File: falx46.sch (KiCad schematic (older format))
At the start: 124 parts, among them J1 USB_C_Receptacle_USB2.0, J2 OLED_I2C, J3 AVR-ISP-6, J4 TRRS_I2C, SW1 SW_PUSH, SW10 SW_PUSH, SW11 SW_PUSH, SW12 SW_PUSH, SW13 SW_PUSH, SW14 SW_PUSH, SW15 SW_PUSH, SW16 SW_PUSH, SW17 SW_PUSH, SW18 SW_PUSH, SW19 Rotary_Encoder_Switch, SW2 SW_PUSH, SW20 SW_PUSH, SW21 SW_PUSH, SW22 SW_PUSH, SW23 SW_PUSH, SW24 SW_PUSH, SW25 SW_PUSH, SW26 SW_PUSH, SW27 SW_PUSH, SW28 SW_PUSH, SW29 SW_PUSH, SW3 SW_PUSH, SW30 SW_PUSH, SW31 SW_PUSH, SW32 SW_PUSH, SW33 SW_PUSH, SW34 SW_PUSH, SW35 SW_PUSH, SW36 Rotary_Encoder_Switch, SW37 SW_PUSH, SW38 SW_PUSH, SW39 SW_PUSH, SW4 SW_PUSH, SW40 SW_PUSH, SW41 SW_PUSH, SW42 SW_PUSH, SW43 SW_PUSH, SW44 SW_PUSH, SW45 SW_PUSH, SW46 SW_PUSH, SW47 SW_Push, SW5 SW_PUSH, SW6 SW_PUSH, SW7 SW_PUSH, SW8 SW_PUSH, SW9 SW_PUSH, U1 ATmega32U4-AU, Y1 16MHz

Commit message: ライブラリの参照を修正
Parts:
- J4: symbol falx46-rescue:MJ-4PP-9-kbd -> foostan_kbd:MJ-4PP-9
- SW1, SW10, SW11, SW12, SW13, SW14, SW15, SW16, SW17, SW18, SW2, SW20, SW21, SW22, SW23, SW24, SW25, SW26, SW27, SW28, SW29, SW3, SW30, SW31, SW32, SW33, SW34, SW35, SW37, SW38, SW39, SW4, SW40, SW41, SW42, SW43, SW44, SW45, SW46, SW5, SW6, SW7, SW8, SW9: symbol falx46-rescue:SW_PUSH-kbd -> foostan_kbd:SW_PUSH
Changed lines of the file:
@@
 COL0
 $Comp
-L falx46-rescue:SW_PUSH-kbd SW1
+L foostan_kbd:SW_PUSH SW1
 U 1 1 5F5B60E2
 P 7450 1400
@@
 $EndComp
 $Comp
-L falx46-rescue:SW_PUSH-kbd SW2
+L foostan_kbd:SW_PUSH SW2
 U 1 1 5F5B6E67
 P 8250 1400
@@
 $EndComp
 $Comp
-L falx46-rescue:SW_PUSH-kbd SW3
+L foostan_kbd:SW_PUSH SW3
 U 1 1 5F5B876D
 P 9050 1400
@@
 $EndComp
 $Comp
-L falx46-rescue:SW_PUSH-kbd SW4
+L foostan_kbd:SW_PUSH SW4
 U 1 1 5F5B8EE0
 P 9850 1400
@@
 $EndComp
 $Comp
-L falx46-rescue:SW_PUSH-kbd SW5
+L foostan_kbd:SW_PUSH SW5
 U 1 1 5F5D5213
 P 10650 1400
@@
 COL6
 $Comp
-L falx46-rescue:SW_PUSH-kbd SW6
+L foostan_kbd:SW_PUSH SW6
 U 1 1 5F5D7903
 P 6600 2100
@@
 $EndComp
 $Comp
-L falx46-rescue:SW_PUSH-kbd SW7
+L foostan_kbd:SW_PUSH SW7
 U 1 1 5F5D856F
 P 7450 2100
@@
 $EndComp
 $Comp
-L falx46-rescue:SW_PUSH-kbd SW8
+L foostan_kbd:SW_PUSH SW8
 U 1 1 5F5D8D10
 P 8250 2100
@@
 $EndComp
 $Comp
-L falx46-rescue:SW_PUSH-kbd SW9
+L foostan_kbd:SW_PUSH SW9
 U 1 1 5F5D95B6
 P 9050 2100
@@
 $EndComp
 $Comp
-L falx46-rescue:SW_PUSH-kbd SW10
+L foostan_kbd:SW_PUSH SW10
 U 1 1 5F5D9E13
 P 9850 2100
@@
 $EndComp
 $Comp
-L falx46-rescue:SW_PUSH-kbd SW11
+L foostan_kbd:SW_PUSH SW11
 U 1 1 5F5DB97E
 P 10650 2100
@@
 $EndComp
 $Comp
-L falx46-rescue:SW_PUSH-kbd SW12
+L foostan_kbd:SW_PUSH SW12
 U 1 1 5F5DC0BA
 P 11450 2100
@@
 	6300 1100 6300 2100
 $Comp
-L falx46-rescue:SW_PUSH-kbd SW13
+L foostan_kbd:SW_PUSH SW13
 U 1 1 5F5F3D5F
 P 6600 2750
@@
 $EndComp
 $Comp
-L falx46-rescue:SW_PUSH-kbd SW14
+L foostan_kbd:SW_PUSH SW14
 U 1 1 5F5F4155
 P 7450 2750
@@
 $EndComp
 $Comp
-L falx46-rescue:SW_PUSH-kbd SW15
+L foostan_kbd:SW_PUSH SW15
 U 1 1 5F5F446B
 P 8250 2750
@@
 $EndComp
 $Comp
-L falx46-rescue:SW_PUSH-kbd SW16
+L foostan_kbd:SW_PUSH SW16
 U 1 1 5F5F485F
 P 9050 2750
@@
 $EndComp
 $Comp
-L falx46-rescue:SW_PUSH-kbd SW17
+L foostan_kbd:SW_PUSH SW17
 U 1 1 5F5F4CB1
 P 9850 2750
@@
 $EndComp
 $Comp
-L falx46-rescue:SW_PUSH-kbd SW18
+L foostan_kbd:SW_PUSH SW18
 U 1 1 5F5F50F9
 P 10650 2750
@@
 	10950 3050 11300 3050
 $Comp
-L falx46-rescue:SW_PUSH-kbd SW20
+L foostan_kbd:SW_PUSH SW20
 U 1 1 5F5FD739
 P 9850 3400
@@
 $EndComp
 $Comp
-L falx46-rescue:SW_PUSH-kbd SW21
+L foostan_kbd:SW_PUSH SW21
 U 1 1 5F5FDB5A
 P 10650 3400
@@
 $EndComp
 $Comp
-L falx46-rescue:SW_PUSH-kbd SW22
+L foostan_kbd:SW_PUSH SW22
 U 1 1 5F5FDECC
 P 11450 3400
@@
 $EndComp
 $Comp
-L falx46-rescue:SW_PUSH-kbd SW23
+L foostan_kbd:SW_PUSH SW23
 U 1 1 5F6013A1
 P 10650 4100
@@
 $EndComp
 $Comp
-L falx46-rescue:SW_PUSH-kbd SW46
+L foostan_kbd:SW_PUSH SW46
 U 1 1 5F68C46B
 P 7450 7850
@@
 $EndComp
 $Comp
-L falx46-rescue:SW_PUSH-kbd SW45
+L foostan_kbd:SW_PUSH SW45
 U 1 1 5F686113
 P 8250 7200
@@
 $EndComp
 $Comp
-L falx46-rescue:SW_PUSH-kbd SW44
+L foostan_kbd:SW_PUSH SW44
 U 1 1 5F685D24
 P 7450 7200
@@
 $EndComp
 $Comp
-L falx46-rescue:SW_PUSH-kbd SW43
+L foostan_kbd:SW_PUSH SW43
 U 1 1 5F685647
 P 6600 7200
@@
 $EndComp
 $Comp
-L falx46-rescue:SW_PUSH-kbd SW42
+L foostan_kbd:SW_PUSH SW42
 U 1 1 5F67A585
 P 11450 6550
@@
 $EndComp
 $Comp
-L falx46-rescue:SW_PUSH-kbd SW41
+L foostan_kbd:SW_PUSH SW41
 U 1 1 5F67A112
 P 10650 6550
@@
 $EndComp
 $Comp
-L falx46-rescue:SW_PUSH-kbd SW40
+L foostan_kbd:SW_PUSH SW40
 U 1 1 5F679C55
 P 9850 6550
@@
 $EndComp
 $Comp
-L falx46-rescue:SW_PUSH-kbd SW39
+L foostan_kbd:SW_PUSH SW39
 U 1 1 5F6797C3
 P 9050 6550
@@
 $EndComp
 $Comp
-L falx46-rescue:SW_PUSH-kbd SW38
+L foostan_kbd:SW_PUSH SW38
 U 1 1 5F6793B1
 P 8250 6550
@@
 $EndComp
 $Comp
-L falx46-rescue:SW_PUSH-kbd SW37
+L foostan_kbd:SW_PUSH SW37
 U 1 1 5F678F73
 P 7450 6550
@@
 $EndComp
 $Comp
-L falx46-rescue:SW_PUSH-kbd SW35
+L foostan_kbd:SW_PUSH SW35
 U 1 1 5F653360
 P 11450 5900
@@
 $EndComp
 $Comp
-L falx46-rescue:SW_PUSH-kbd SW34
+L foostan_kbd:SW_PUSH SW34
 U 1 1 5F652E0C
 P 10650 5900
@@
 $EndComp
 $Comp
-L falx46-rescue:SW_PUSH-kbd SW33
+L foostan_kbd:SW_PUSH SW33
 U 1 1 5F6528E6
 P 9850 5900
@@
 $EndComp
 $Comp
-L falx46-rescue:SW_PUSH-kbd SW32
+L foostan_kbd:SW_PUSH SW32
 U 1 1 5F65245C
 P 9050 5900
@@
 $EndComp
 $Comp
-L falx46-rescue:SW_PUSH-kbd SW31
+L foostan_kbd:SW_PUSH SW31
 U 1 1 5F651F57
 P 8250 5900
@@
 $EndComp
 $Comp
-L falx46-rescue:SW_PUSH-kbd SW30
+L foostan_kbd:SW_PUSH SW30
 U 1 1 5F651BB2
 P 7450 5900
@@
 $EndComp
 $Comp
-L falx46-rescue:SW_PUSH-kbd SW29
+L foostan_kbd:SW_PUSH SW29
 U 1 1 5F651603
 P 6600 5900
@@
 $EndComp
 $Comp
-L falx46-rescue:SW_PUSH-kbd SW28
+L foostan_kbd:SW_PUSH SW28
 U 1 1 5F62D006
 P 10650 5250
@@
 $EndComp
 $Comp
-L falx46-rescue:SW_PUSH-kbd SW27
+L foostan_kbd:SW_PUSH SW27
 U 1 1 5F62C98B
 P 9850 5250
@@
 $EndComp
 $Comp
-L falx46-rescue:SW_PUSH-kbd SW26
+L foostan_kbd:SW_PUSH SW26
 U 1 1 5F62C423
 P 9050 5250
@@
 $EndComp
 $Comp
-L falx46-rescue:SW_PUSH-kbd SW25
+L foostan_kbd:SW_PUSH SW25
 U 1 1 5F62BD0C
 P 8250 5250
@@
 $EndComp
 $Comp
-L falx46-rescue:SW_PUSH-kbd SW24
+L foostan_kbd:SW_PUSH SW24
 U 1 1 5F626DF7
 P 7450 5250
@@
 $EndComp
 $Comp
-L falx46-rescue:MJ-4PP-9-kbd J4
+L foostan_kbd:MJ-4PP-9 J4
 U 1 1 60A4AE0C
 P 2750 8325

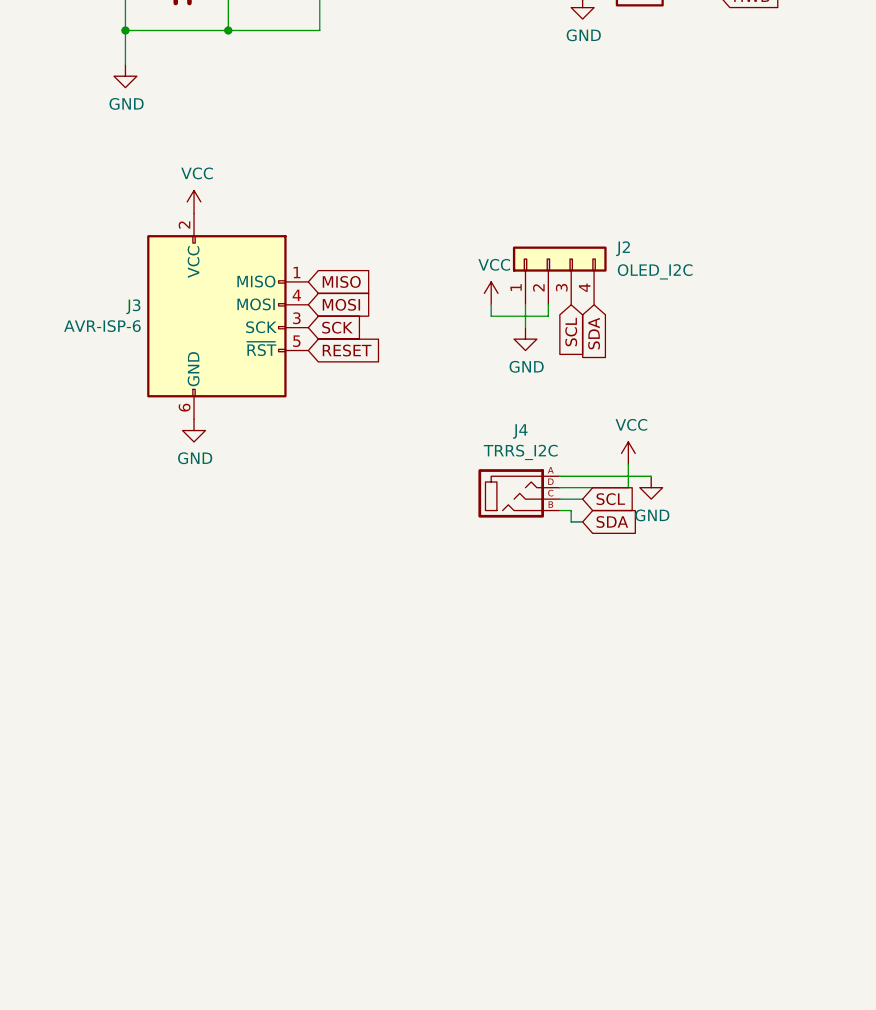
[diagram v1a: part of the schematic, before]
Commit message: 回路図を更新
- Grove I2C端子用ホールを追加
- LEDテープ用接点を追加
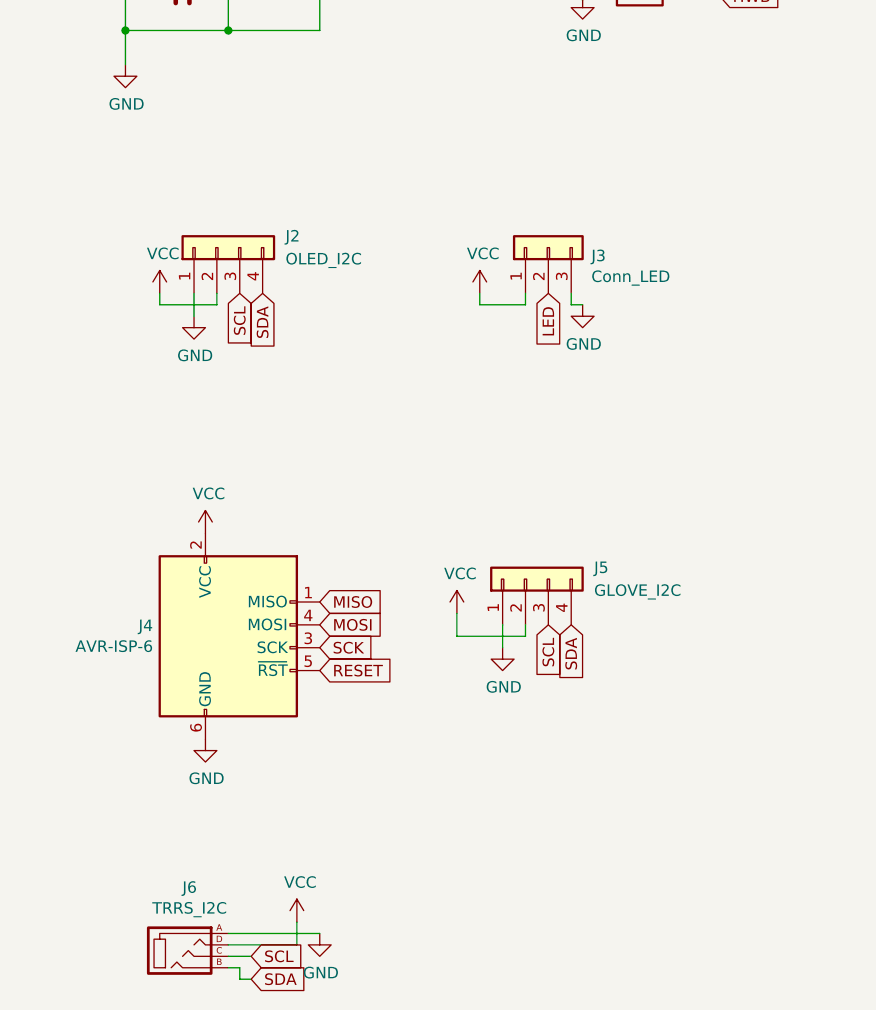
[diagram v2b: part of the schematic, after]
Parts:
- added J3: Conn_LED, foostan-kbd:StripLED_1side, symbol Connector_Generic:Conn_01x03
- added J5: GLOVE_I2C, 1m38_kbd:Grove_I2C, symbol Connector_Generic:Conn_01x04
- C1, C2, C3, C4: footprint Capacitor_SMD:C_0603_1608Metric_Pad1.05x0.95mm_HandSolder -> Capacitor_SMD:C_0805_2012Metric_Pad1.15x1.40mm_HandSolder
- J6: renamed from J4; footprint foostan-kbd:MJ-4PP-9_1side -> 1m38_kbd:MJ-4PP-9_1side_backside-mask
- renumbered J3 to J4
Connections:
- net GND: now also J3.3 (Pin_3), J5.1 (Pin_1)
- net LED: now also J3.2 (Pin_2)
- net SCL: now also J5.3 (Pin_3)
- net SDA: now also J5.4 (Pin_4)
- net VCC: now also J3.1 (Pin_1), J5.2 (Pin_2)
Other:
- moved on the sheet: J2, J4, J6

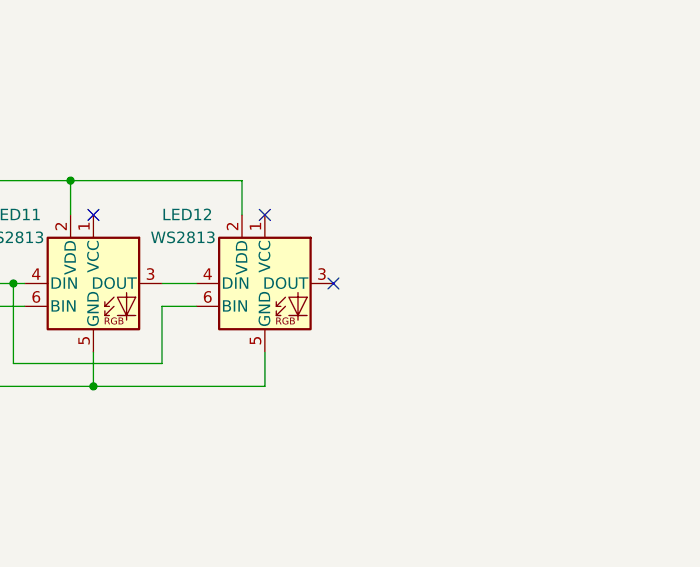
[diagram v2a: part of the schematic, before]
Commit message: LEDを2つ追加
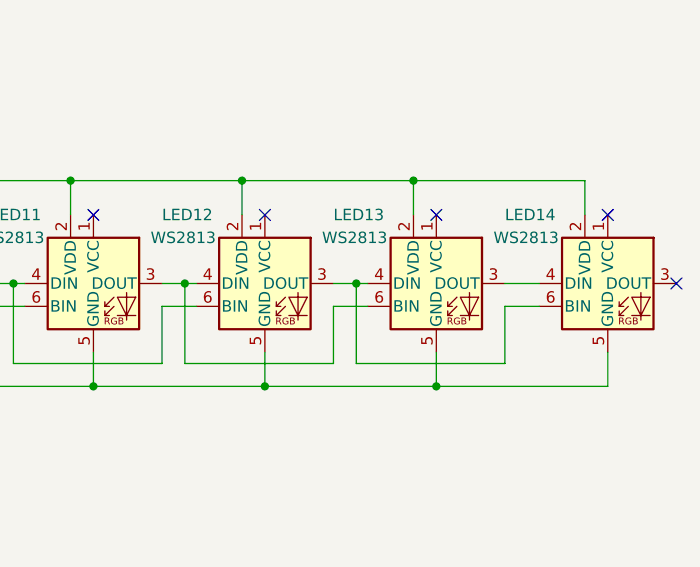
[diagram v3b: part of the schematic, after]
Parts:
- added LED13, LED14: WS2813, LED_SMD:LED_WS2812_PLCC6_5.0x5.0mm_P1.6mm, symbol LED:WS2813
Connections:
- net GND: now also LED13.5 (GND), LED14.5 (GND)
- net VCC: now also LED13.2 (VDD), LED14.2 (VDD)
- net at LED11.3 (DOUT), LED12.4 (DIN): now also LED13.6 (BIN)
- net at LED12.3 (DOUT): now also LED13.4 (DIN), LED14.6 (BIN)
- new net: LED13.3 (DOUT), LED14.4 (DIN)
- no-connect marks 18 -> 20
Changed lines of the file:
@@
 Connection ~ 12650 8500
 Wire Wire Line
-	13050 8950 13200 8950
+	13050 8950 13150 8950
 Wire Wire Line
 	12300 8950 12400 8950
@@
 Wire Wire Line
 	12400 8950 12450 8950
-NoConn ~ 13800 8950
+NoConn ~ 15300 8950
 NoConn ~ 13500 8650
 NoConn ~ 12750 8650
@@
 Wire Wire Line
 	3000 7500 3050 7500
+$Comp
+L LED:WS2813 LED13
+U 1 1 5F630244
+P 14250 8950
+F 0 "LED13" H 13800 9250 50  0000 L CNN
+F 1 "WS2813" H 13750 9150 50  0000 L CNN
+F 2 "LED_SMD:LED_WS2812_PLCC6_5.0x5.0mm_P1.6mm" H 14300 8650 50  0001 L TNN
+F 3 "http://www.normandled.com/upload/201605/WS2813%20LED%20Datasheet.pdf" H 14350 8575 50  0001 L TNN
+	1    14250 8950
+	1    0    0    -1
+$EndComp
+$Comp
+L LED:WS2813 LED14
+U 1 1 5F630AA9
+P 15000 8950
+F 0 "LED14" H 14550 9250 50  0000 L CNN
+F 1 "WS2813" H 14500 9150 50  0000 L CNN
+F 2 "LED_SMD:LED_WS2812_PLCC6_5.0x5.0mm_P1.6mm" H 15050 8650 50  0001 L TNN
+F 3 "http://www.normandled.com/upload/201605/WS2813%20LED%20Datasheet.pdf" H 15100 8575 50  0001 L TNN
+	1    15000 8950
+	1    0    0    -1
+$EndComp
+Wire Wire Line
+	13800 8950 13900 8950
+Wire Wire Line
+	14550 8950 14700 8950
+Wire Wire Line
+	13150 8950 13150 9300
+Wire Wire Line
+	13150 9300 13800 9300
+Wire Wire Line
+	13800 9300 13800 9050
+Wire Wire Line
+	13800 9050 13950 9050
+Connection ~ 13150 8950
+Wire Wire Line
+	13150 8950 13200 8950
+Wire Wire Line
+	13900 8950 13900 9300
+Wire Wire Line
+	13900 9300 14550 9300
+Wire Wire Line
+	14550 9300 14550 9050
+Wire Wire Line
+	14550 9050 14700 9050
+Connection ~ 13900 8950
+Wire Wire Line
+	13900 8950 13950 8950
+Wire Wire Line
+	13500 9400 14250 9400
+Wire Wire Line
+	14250 9400 14250 9250
+Connection ~ 13500 9400
+Wire Wire Line
+	14250 9400 15000 9400
+Wire Wire Line
+	15000 9400 15000 9250
+Connection ~ 14250 9400
+Wire Wire Line
+	13400 8500 14150 8500
+Wire Wire Line
+	14150 8500 14150 8650
+Connection ~ 13400 8500
+Wire Wire Line
+	14150 8500 14900 8500
+Wire Wire Line
+	14900 8500 14900 8650
+Connection ~ 14150 8500
+NoConn ~ 14250 8650
+NoConn ~ 15000 8650
 $EndSCHEMATC

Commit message: 仮配線
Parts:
- removed J3: Conn_LED, foostan-kbd:StripLED_1side, symbol Connector_Generic:Conn_01x03
- J1: footprint Connector_USB:USB_C_Receptacle_GCT_USB4085 -> 1m38_kbd:USB_C_Receptacle_GCT_USB4085
- SW1, SW10, SW11, SW12, SW13, SW14, SW15, SW16, SW17, SW18, SW2, SW20, SW21, SW22, SW23, SW24, SW25, SW26, SW27, SW28, SW29, SW3, SW30, SW31, SW32, SW33, SW34, SW35, SW37, SW38, SW39, SW4, SW40, SW41, SW42, SW43, SW44, SW45, SW46, SW5, SW6, SW7, SW8, SW9: footprint ai03-kbd-MX:MXOnly-1U-Hotswap-Antishear -> 1m38_kbd:MXOnly-1U-Hotswap-Antishear-mod
- renumbered J4 to J3, J5 to J4, J6 to J5
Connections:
- net COL0: no longer U1.38 (PF5)
- net COL1: no longer U1.37 (PF6)
- net COL2: no longer U1.36 (PF7)
- net COL3: no longer U1.32 (PC7)
- net COL4: no longer U1.31 (PC6)
- net COL5: no longer U1.30 (PB6)
- net COL6: no longer U1.25 (PD4), U1.29 (PB5)
- net ENCL1: no longer U1.39 (PF4)
- net ENCL2: no longer U1.40 (PF1)
- net ENCR1: no longer U1.20 (PD2)
- net ENCR2: no longer U1.21 (PD3)
- net GND: now also J4.4 (Pin_4); no longer J4.1 (Pin_1)
- net LED: no longer U1.1 (PE6)
- net MISO: no longer D20.1 (K), D21.1 (K), D22.1 (K), D23.1 (K)
- net MOSI: no longer D13.1 (K), D14.1 (K), D15.1 (K), D16.1 (K), D17.1 (K), D18.1 (K), D19.1 (K)
- net ROWL0: no longer U1.8 (PB0)
- net ROWL1: no longer J3.3 (SCK), U1.9 (PB1)
- net ROWR0: no longer U1.28 (PB4)
- net ROWR1: no longer U1.27 (PD7)
- net ROWR2: no longer U1.26 (PD6)
- net SCL: now also J4.2 (Pin_2); no longer J4.3 (Pin_3)
- net SDA: now also J4.1 (Pin_1); no longer J4.4 (Pin_4)
- net VCC: now also J4.3 (Pin_3); no longer J4.2 (Pin_2)
- net DUP: now reaches J1.A6 (D+), J1.B6 (D+), R4.1
- net DUN: now reaches J1.A7 (D-), J1.B7 (D-), R3.2
- new net ROWL2: D13.1 (K), D14.1 (K), D15.1 (K), D16.1 (K), D17.1 (K), D18.1 (K), D19.1 (K)
- new net ROWL3: D20.1 (K), D21.1 (K), D22.1 (K), D23.1 (K)
- new net SCK: J3.3 (SCK), U1.9 (PB1)
- no-connect marks 20 -> 57
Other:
- moved on the sheet: R4

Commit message: 一旦配線を完了
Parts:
- SW1, SW10, SW11, SW12, SW13, SW14, SW15, SW16, SW17, SW18, SW2, SW20, SW21, SW22, SW23, SW24, SW25, SW26, SW27, SW28, SW29, SW3, SW30, SW31, SW32, SW33, SW34, SW35, SW37, SW38, SW39, SW4, SW40, SW41, SW42, SW43, SW44, SW45, SW46, SW5, SW6, SW7, SW8, SW9: footprint 1m38_kbd:MXOnly-1U-Hotswap-Antishear-mod -> 1m38_kbd:CherryMX_Hotswap_mod
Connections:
- net COL6: no longer D43.1 (K), D44.1 (K), D45.1 (K), D46.1 (K)
- new net ROWR3: D43.1 (K), D44.1 (K), D45.1 (K), D46.1 (K)

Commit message: 配線完了
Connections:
- net ROWR0 is gone; now on net MISO: D24.1 (K), D25.1 (K), D26.1 (K), D27.1 (K), D28.1 (K)
- net ROWR1 is gone; now on net MOSI: D29.1 (K), D30.1 (K), D31.1 (K), D32.1 (K), D33.1 (K), D34.1 (K), D35.1 (K)
- net SCK is gone; now on net ROWR2: J3.3 (SCK), U1.9 (PB1)
- net COL0: now also U1.21 (PD3)
- net COL1: now also U1.22 (PD5)
- net COL2: now also U1.25 (PD4)
- net COL3: now also U1.26 (PD6)
- net COL4: now also U1.27 (PD7)
- net COL5: now also U1.28 (PB4)
- net COL6: now also U1.29 (PB5)
- net ENCL1: now also U1.38 (PF5)
- net ENCL2: now also U1.39 (PF4)
- net ENCR1: now also U1.41 (PF0)
- net ENCR2: now also U1.40 (PF1)
- net LED: now also U1.30 (PB6)
- net ROWL0: now also U1.37 (PF6)
- net ROWL1: now also U1.36 (PF7)
- net ROWL2: now also U1.32 (PC7)
- net ROWL3: now also U1.31 (PC6)
- net ROWR3: now also U1.8 (PB0)
- no-connect marks 57 -> 20
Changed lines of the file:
@@
 Wire Wire Line
 	10350 4100 8750 4100
-Text GLabel 5050 1450 2    50   Input ~ 0
-SCK
-Text GLabel 5050 1550 2    50   Input ~ 0
-MOSI
-Text GLabel 5050 1650 2    50   Input ~ 0
-MISO
 $Comp
 L Device:Rotary_Encoder_Switch SW19
@@
 NoConn ~ 8250 8650
 NoConn ~ 7500 8650
-Connection ~ 3950 4600
 Wire Wire Line
 	3850 4600 3950 4600
@@
 	3850 1000 3950 1000
 Wire Wire Line
-	3950 900  3950 1000
-$Comp
-L MCU_Microchip_ATmega:ATmega32U4-AU U1
-U 1 1 5F524E5E
-P 3950 2800
-F 0 "U1" H 3100 1350 50  0000 C CNN
-F 1 "ATmega32U4-AU" H 3100 1250 50  0000 C CNN
-F 2 "Package_QFP:TQFP-44_10x10mm_P0.8mm" H 3950 2800 50  0001 C CIN
-F 3 "http://ww1.microchip.com/downloads/en/DeviceDoc/Atmel-7766-8-bit-AVR-ATmega16U4-32U4_Datasheet.pdf" H 3950 2800 50  0001 C CNN
-	1    3950 2800
-	1    0    0    -1
-$EndComp
-Wire Wire Line
 	4550 1400 4600 1400
 Wire Wire Line
@@
 Wire Wire Line
 	4600 1600 4600 1650
-Text GLabel 4750 4600 2    50   Input ~ 0
+Text GLabel 4550 2800 2    50   Input ~ 0
 COL0
-Text GLabel 4750 4750 2    50   Input ~ 0
+Text GLabel 4550 3000 2    50   Input ~ 0
 COL1
-Text GLabel 4750 4900 2    50   Input ~ 0
+Text GLabel 4550 2900 2    50   Input ~ 0
 COL2
-Text GLabel 4750 5050 2    50   Input ~ 0
+Text GLabel 4550 3100 2    50   Input ~ 0
 COL3
-Text GLabel 4750 5200 2    50   Input ~ 0
+Text GLabel 4550 3200 2    50   Input ~ 0
 COL4
-Text GLabel 4750 5350 2    50   Input ~ 0
+Text GLabel 4550 1700 2    50   Input ~ 0
 COL5
-Text GLabel 4750 5500 2    50   Input ~ 0
+Text GLabel 4550 1800 2    50   Input ~ 0
 COL6
-Text GLabel 4750 6000 2    50   Input ~ 0
+Text GLabel 4550 3700 2    50   Input ~ 0
 ENCR1
-Text GLabel 4750 6150 2    50   Input ~ 0
+Text GLabel 4550 3800 2    50   Input ~ 0
 ENCR2
-Text GLabel 4750 5700 2    50   Input ~ 0
+Text GLabel 4550 4000 2    50   Input ~ 0
 ENCL1
-Text GLabel 4750 5850 2    50   Input ~ 0
+Text GLabel 4550 3900 2    50   Input ~ 0
 ENCL2
-Text GLabel 4750 4450 2    50   Input ~ 0
+Text GLabel 4550 1900 2    50   Input ~ 0
 LED
-NoConn ~ 4550 3700
 Wire Wire Line
 	1750 1300 1750 1450
@@
 Wire Wire Line
 	4600 1450 5050 1450
-NoConn ~ 4550 1300
-NoConn ~ 4550 1700
-NoConn ~ 4550 1800
-NoConn ~ 4550 1900
-NoConn ~ 4550 2200
-NoConn ~ 4550 2300
-NoConn ~ 4550 2900
-NoConn ~ 4550 3100
-NoConn ~ 4550 3200
 NoConn ~ 4550 3500
-NoConn ~ 4550 3800
-NoConn ~ 4550 3900
-NoConn ~ 4550 4000
-NoConn ~ 4550 4100
-NoConn ~ 4550 4200
-NoConn ~ 4750 4450
-NoConn ~ 4750 4600
-NoConn ~ 4750 4750
-NoConn ~ 4750 4900
-NoConn ~ 4750 5050
-NoConn ~ 4750 5200
-NoConn ~ 4750 5350
-NoConn ~ 4750 5500
-NoConn ~ 4750 5700
-NoConn ~ 4750 5850
-NoConn ~ 4750 6000
-NoConn ~ 4750 6150
 Text Label 1850 2100 0    50   ~ 0
 DUN
@@
 Wire Wire Line
 	3200 8950 3200 8900
-NoConn ~ 5300 5350
-NoConn ~ 5300 5200
-NoConn ~ 5300 5050
-NoConn ~ 5300 4900
-Text GLabel 5300 4900 2    50   Input ~ 0
+Text GLabel 4650 1600 2    50   Input ~ 0
 ROWR0
-Text GLabel 5300 5350 2    50   Input ~ 0
+Text GLabel 4550 1300 2    50   Input ~ 0
 ROWR3
-Text GLabel 5300 5200 2    50   Input ~ 0
+Text GLabel 4650 1400 2    50   Input ~ 0
 ROWR2
-Text GLabel 5300 5050 2    50   Input ~ 0
+Text GLabel 4650 1500 2    50   Input ~ 0
 ROWR1
+Text GLabel 4550 4200 2    50   Input ~ 0
+ROWL1
+Text GLabel 4550 2300 2    50   Input ~ 0
+ROWL2
+Text GLabel 4550 2200 2    50   Input ~ 0
+ROWL3
+Wire Wire Line
+	6100 7500 6900 7500
+Text GLabel 4550 4100 2    50   Input ~ 0
+ROWL0
+Text GLabel 5050 1650 2    50   Input ~ 0
+MISO
+Text GLabel 5050 1550 2    50   Input ~ 0
+MOSI
+Text GLabel 5050 1450 2    50   Input ~ 0
+SCK
+Wire Wire Line
+	4650 1400 4600 1400
+Connection ~ 4600 1400
+Wire Wire Line
+	4650 1500 4600 1500
+Connection ~ 4600 1500
+Wire Wire Line
+	4650 1600 4600 1600
+Connection ~ 4600 1600
 NoConn ~ 4550 2000
 NoConn ~ 4550 2700
-NoConn ~ 4550 2800
-NoConn ~ 5300 4550
-NoConn ~ 5300 4400
-NoConn ~ 5300 4250
-Text GLabel 5300 4250 2    50   Input ~ 0
-ROWL1
-Text GLabel 5300 4400 2    50   Input ~ 0
-ROWL2
-Text GLabel 5300 4550 2    50   Input ~ 0
-ROWL3
-NoConn ~ 5300 4100
-Wire Wire Line
-	6100 7500 6900 7500
-NoConn ~ 4550 3000
-Text GLabel 5300 4100 2    50   Input ~ 0
-ROWL0
+Connection ~ 3950 4600
+Wire Wire Line
+	3950 900  3950 1000
+$Comp
+L MCU_Microchip_ATmega:ATmega32U4-AU U1
+U 1 1 5F524E5E
+P 3950 2800
+F 0 "U1" H 3100 1350 50  0000 C CNN
+F 1 "ATmega32U4-AU" H 3100 1250 50  0000 C CNN
+F 2 "Package_QFP:TQFP-44_10x10mm_P0.8mm" H 3950 2800 50  0001 C CIN
+F 3 "http://ww1.microchip.com/downloads/en/DeviceDoc/Atmel-7766-8-bit-AVR-ATmega16U4-32U4_Datasheet.pdf" H 3950 2800 50  0001 C CNN
+	1    3950 2800
+	1    0    0    -1
+$EndComp
 $EndSCHEMATC

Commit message: シルク調整中
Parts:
- D1, D10, D11, D12, D13, D14, D15, D16, D17, D18, D19, D2, D20, D21, D22, D23, D24, D25, D26, D27, D28, D29, D3, D30, D31, D32, D33, D34, D35, D36, D37, D38, D39, D4, D40, D41, D42, D43, D44, D45, D46, D5, D6, D7, D8, D9: footprint foostan-kbd:D3_SMD_v2 -> 1m38_kbd:D3_SMD_v2_silk
- J5: footprint 1m38_kbd:MJ-4PP-9_1side_backside-mask -> 1m38_kbd:MJ-4PP-9_1side_no-mask
